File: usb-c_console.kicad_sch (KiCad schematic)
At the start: 28 parts, among them J3 USB-C_Kycon_KUSBX-SL2-CS1N24-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, U6 FT230X_QFN, U7 NTS0102_TSSOP

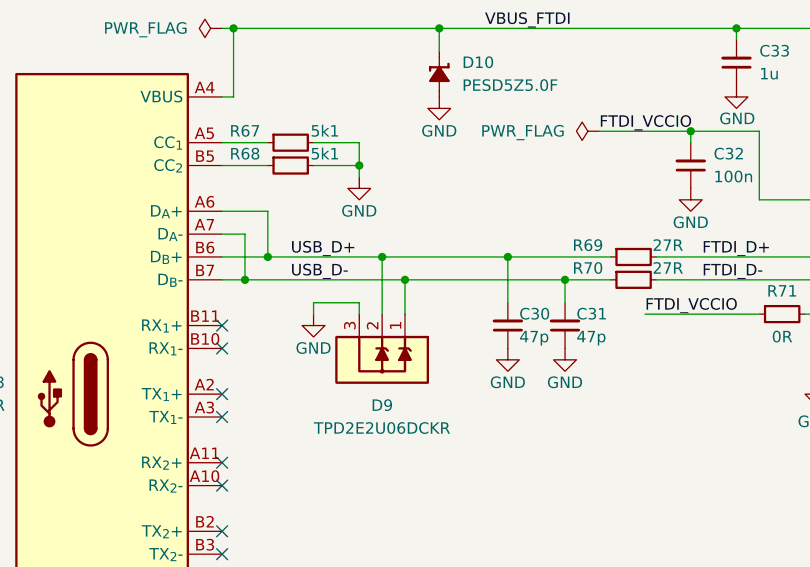
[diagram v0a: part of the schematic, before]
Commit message: [#65840] Layout FTDI
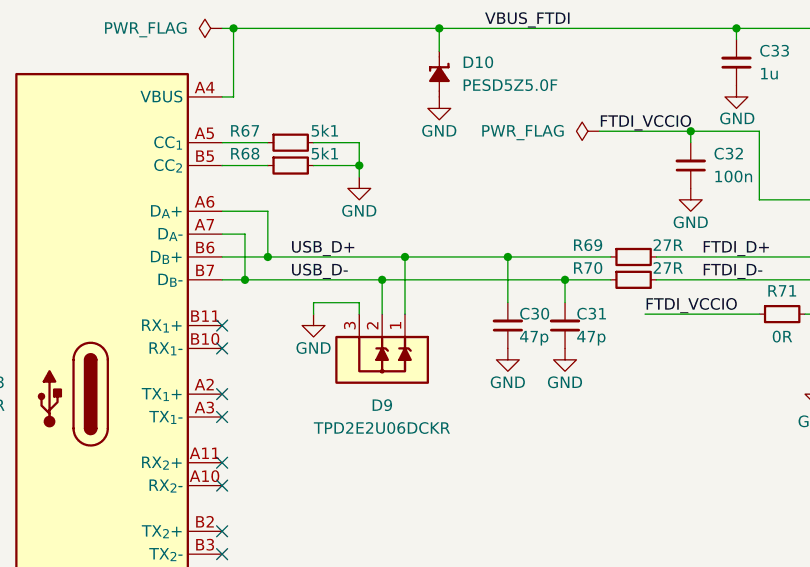
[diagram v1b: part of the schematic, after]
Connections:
- net USB_D+: now also D9.1; no longer D9.2
- net USB_D-: now also D9.2; no longer D9.1
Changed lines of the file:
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@@
   (junction (at 124.46 111.76) (diameter 0) (color 0 0 0 0)
   )
-  (junction (at 140.97 137.16) (diameter 0) (color 0 0 0 0)
-  )
   (junction (at 124.46 191.77) (diameter 0) (color 0 0 0 0)
   )
@@
   (junction (at 189.23 130.81) (diameter 0) (color 0 0 0 0)
   )
+  (junction (at 140.97 139.7) (diameter 0) (color 0 0 0 0)
+  )
   (junction (at 232.41 130.81) (diameter 0) (color 0 0 0 0)
   )
@@
   (junction (at 262.89 111.76) (diameter 0) (color 0 0 0 0)
   )
-  (junction (at 143.51 139.7) (diameter 0) (color 0 0 0 0)
+  (junction (at 143.51 137.16) (diameter 0) (color 0 0 0 0)
   )
   (junction (at 289.56 125.73) (diameter 0) (color 0 0 0 0)
@@
     (stroke (width 0) (type default))
   )
+  (wire (pts (xy 143.51 137.16) (xy 143.51 143.51))
+    (stroke (width 0) (type default))
+  )
   (wire (pts (xy 266.7 111.76) (xy 266.7 125.73))
     (stroke (width 0) (type default))
@@
     (stroke (width 0) (type default))
   )
-  (wire (pts (xy 140.97 137.16) (xy 154.94 137.16))
+  (wire (pts (xy 128.27 137.16) (xy 143.51 137.16))
     (stroke (width 0) (type default))
   )
@@
     (stroke (width 0) (type default))
   )
-  (wire (pts (xy 143.51 139.7) (xy 143.51 143.51))
-    (stroke (width 0) (type default))
-  )
   (wire (pts (xy 227.33 123.19) (xy 229.87 123.19))
     (stroke (width 0) (type default))
@@
     (stroke (width 0) (type default))
   )
+  (wire (pts (xy 140.97 139.7) (xy 140.97 143.51))
+    (stroke (width 0) (type default))
+  )
   (wire (pts (xy 171.45 137.16) (xy 190.5 137.16))
     (stroke (width 0) (type default))
@@
     (stroke (width 0) (type default))
   )
-  (wire (pts (xy 140.97 137.16) (xy 140.97 143.51))
-    (stroke (width 0) (type default))
-  )
   (wire (pts (xy 180.34 111.76) (xy 189.23 111.76))
     (stroke (width 0) (type default))
@@
     (stroke (width 0) (type default))
   )
-  (wire (pts (xy 128.27 137.16) (xy 140.97 137.16))
-    (stroke (width 0) (type default))
-  )
   (wire (pts (xy 130.81 205.74) (xy 124.46 205.74))
     (stroke (width 0) (type default))
@@
     (stroke (width 0) (type default))
   )
-  (wire (pts (xy 143.51 139.7) (xy 161.29 139.7))
+  (wire (pts (xy 140.97 139.7) (xy 161.29 139.7))
     (stroke (width 0) (type default))
   )
@@
     (stroke (width 0) (type default))
   )
-  (wire (pts (xy 125.73 139.7) (xy 143.51 139.7))
+  (wire (pts (xy 125.73 139.7) (xy 140.97 139.7))
     (stroke (width 0) (type default))
   )
@@
     (stroke (width 0) (type default))
   )
+  (wire (pts (xy 143.51 137.16) (xy 154.94 137.16))
+    (stroke (width 0) (type default))
+  )

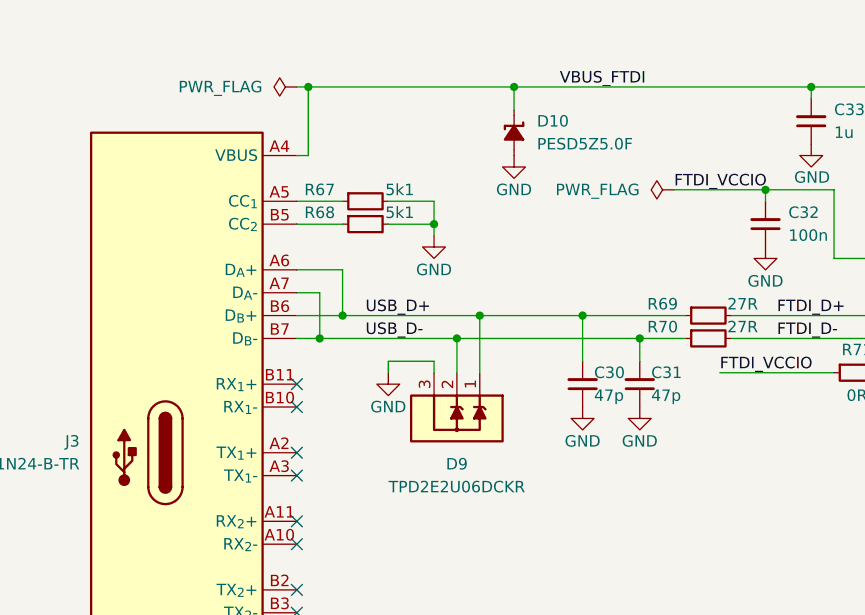
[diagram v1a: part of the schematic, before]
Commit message: [#66613] Fix ERC, adjust overlapping text on schematic
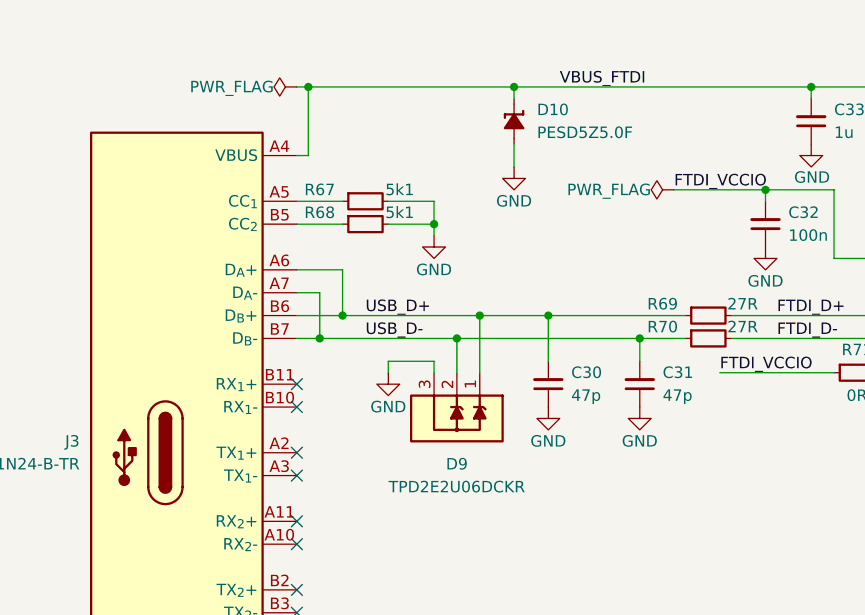
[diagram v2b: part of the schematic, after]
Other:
- moved on the sheet: C30, D10
